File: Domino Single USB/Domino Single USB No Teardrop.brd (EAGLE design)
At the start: 10.2 x 30.5 mm, 15 parts, among them J1 MH4-1

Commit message: Changed copyright
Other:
- board text added: "Reference designs are provided "AS IS" and "WITH ALL FAULTS". The Domino Team disclaims all other warranties express or implied, regarding this product, including but not limited to, any implied warranties of merchantibility or fitness for any particular application."
- board text added: "The Domino Team may make changes to specifications and product descriptions at any time, without notice."
- board text added: "© 2014, The Domino Team. All rights reserved."
- board text removed: "Michel Stempin may make changes to specifications and product descriptions at any time, without notice."
- board text removed: "Reference designs are provided "AS IS" and "WITH ALL FAULTS". Michel Stempin disclaims all other warranties express or implied, regarding this product, including but not limited to, any implied warranties of merchantibility or fitness for any particular application."
- board text removed: "© 2014, Michel Stempin. All rights reserved."
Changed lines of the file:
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@@
 See creativecommons.org/licenses/by-sa/4.0/</text>
 <text x="34.29" y="-51.943" size="0.8128" layer="48" ratio="20">Reference designs are provided "AS IS" and "WITH ALL FAULTS".
-Michel Stempin disclaims all other warranties express or implied,
+The Domino Team disclaims all other warranties express or implied,
 regarding this product, including but not limited to, any implied warranties of
 merchantibility or fitness for any particular application.</text>
-<text x="34.29" y="-55.753" size="0.8128" layer="48" ratio="20">Michel Stempin may make changes to specifications and product descriptions
+<text x="34.29" y="-55.753" size="0.8128" layer="48" ratio="20">The Domino Team may make changes to specifications and product descriptions
 at any time, without notice.</text>
-<text x="74.93" y="-41.91" size="1.27" layer="48" ratio="20">© 2014, Michel Stempin.
+<text x="74.93" y="-41.91" size="1.27" layer="48" ratio="20">© 2014, The Domino Team.
 All rights reserved.</text>
 <text x="115.57" y="-57.15" size="1.778" layer="48">Rev.</text>

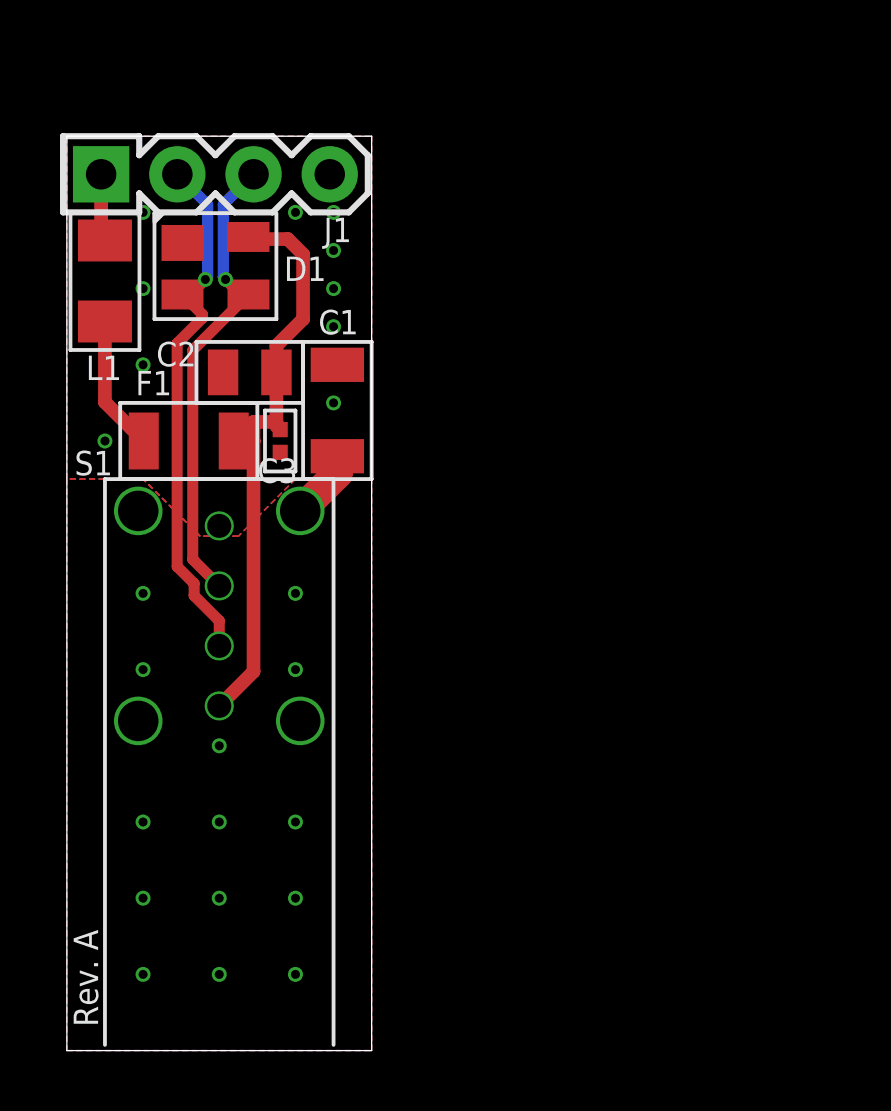
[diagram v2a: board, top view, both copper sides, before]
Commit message: Domino Single USB tile Revision B
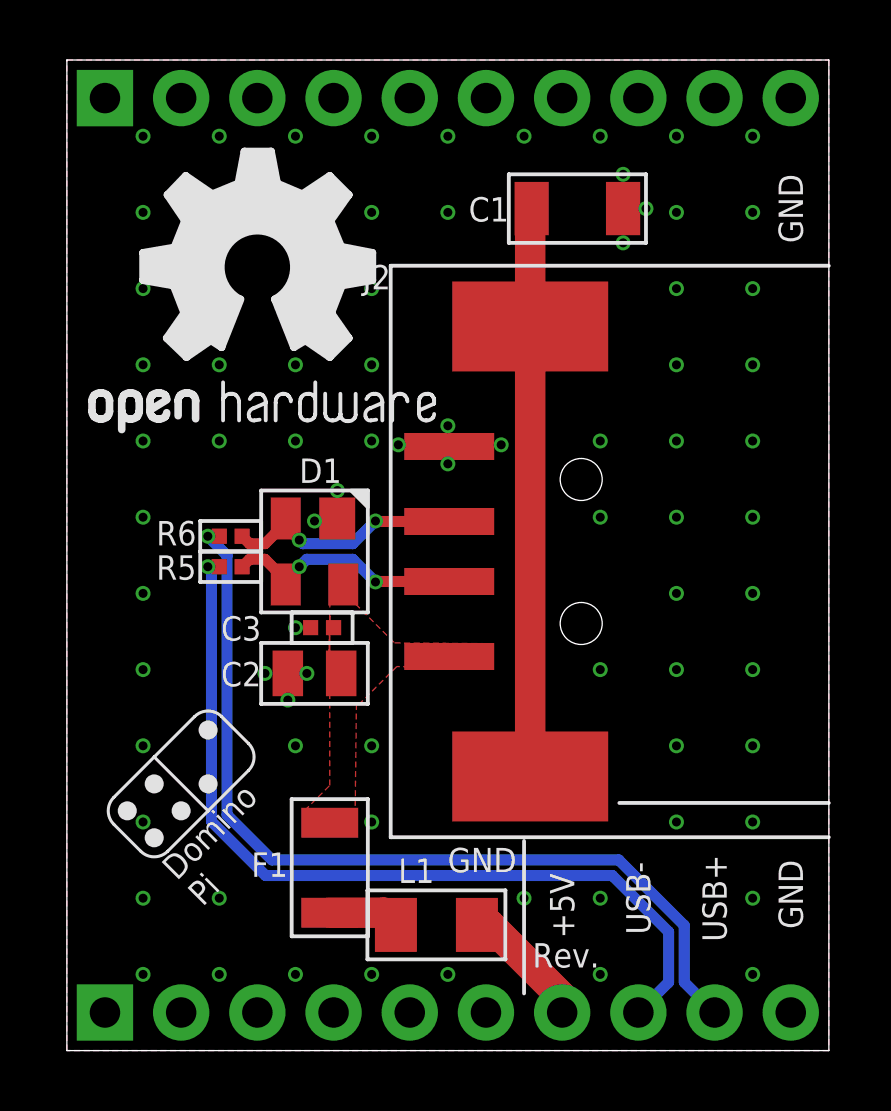
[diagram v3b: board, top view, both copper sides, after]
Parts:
- removed S1: USB_AF-020, Domino:USB_AF-020
- added J2: USB_AF-006, Domino:USB_AF-006
- added J3: MH10-1, Domino:MH10-1-0.1
- added R5, R6: 0R, Domino:R0402
- added U$1: (no value), Domino:ROHS_LOGO
- added U$10: (no value), Domino:DOMINO_LOGO_SMALL
- added U$11: (no value), Domino:ESD_LOGO
- added U$13: (no value), Domino:OPEN_HARDWARE_LOGO
- D1: value YSSR05 -> PRTR5V0U2X
- J1: value MH4-1 -> MH10-1; device Domino:MH4-1-0.1 -> Domino:MH10-1-0.1
- moved J1 27.9 mm to (1.27, 1.27), flipped to the bottom, turned to 180 degrees
- moved L1 24.1 mm to (12.3, 4.19), turned to 180 degrees
- moved F1 15.0 mm to (8.76, 6.10), turned to 90 degrees
- moved U$4 14.4 mm to (13.3, 16.5)
- moved C1 10.5 mm to (17.0, 28.1), turned to 0 degrees
- moved C2 10.3 mm to (8.26, 12.6)
- moved D1 10.1 mm to (8.26, 16.6), turned to 180 degrees
- moved U$6 7.75 mm to (7.24, 11.3)
- moved C3 6.38 mm to (8.51, 14.1), turned to 180 degrees
- moved U$5 5.53 mm to (7.24, 17.7)
- moved U$8 2.84 mm to (6.99, 3.81)
- moved DRILEGEND 1.27 mm to (81.5, 59.9)
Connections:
- removed net +VUSB: J1.1, L1.1
- new net +5V: J1.7, L1.1
- new net USB_N: J1.8, R5.2
- new net USB_P: J1.9, R6.2
- net D_N: now also D1.3, J2.2, R5.1; no longer D1.2, J1.2, S1.2
- net D_P: now also D1.2, J2.3, R6.1; no longer D1.3, J1.3, S1.3
- net GND: now also J1.10, J1.6, J2.4, J3.10; no longer J1.4, S1.4
- net PE: now also J2.S$1, J2.S$2; no longer S1.G$1, S1.G$2, S1.G$3, S1.G$4
- net VBUS: now also J2.1; no longer S1.1
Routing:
- net USB_P: track 0.00 -> 30.0 mm, vias 0 -> 1
- net USB_N: track 0.00 -> 28.8 mm, vias 0 -> 1
- net VBUS: track 19.7 -> 0.00 mm
- net PE: track 2.33 -> 19.0 mm, vias 14 -> 0
- net D_N: track 17.8 -> 8.19 mm, vias 1 -> 2
- net D_P: track 15.8 -> 8.07 mm, vias 1 -> 2
- net +5V: track 0.00 -> 4.35 mm
- net +VUSB: track 2.26 -> 0.00 mm
- net VPROT: track 4.52 -> 2.37 mm
- added copper zone on layer 1, net VBUS
- removed copper zone on layer 1, net PE
- removed copper zone on layer 16, net PE
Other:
- board size 10.2 x 30.5 mm -> 25.4 x 33 mm
- board text added: "01-20"
- board text removed: "Rev. A"
